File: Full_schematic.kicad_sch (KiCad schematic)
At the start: 165 parts, among them IC1 XC7A100T-1FTG256C, IC2 STM32U545VET6Q, J4 Conn_ST_STDC14, J5 Conn_ST_STDC14, SW1 SW_Nidec_CAS-120A1, U2 TPS54294PWP, U2 TPS54325PWPR, U3 SN74ALVC245PWR, U4 SN74ALVC245PWR, U5 STM32F745VGH6, Y1 ASCO, Y2 8MHz, Y3 8MHz

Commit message: koble vga-fpga
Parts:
- removed C62, C75: 1 uF, symbol Device:C
- removed C63, C65, C66, C67, C69, C76, C78, C79, C80, C81: 100 nF, symbol Device:C
- removed C64, C77: 4.7 uF, symbol Device:C
- removed C68, C70, C73, C74: 22pF, symbol Device:C
- removed C71, C72, C82, C83: 2.2u, symbol Device:C
- removed IC2: STM32U545VET6Q, QFP50P1600X1600X160-100N, symbol STM32U545VET6Q:STM32U545VET6Q
- removed J4, J5: Conn_ST_STDC14, symbol Connector:Conn_ST_STDC14
- removed R53, R54: 10k, symbol Device:R
- removed SW1: SW_Nidec_CAS-120A1, Button_Switch_SMD:Nidec_Copal_CAS-120A, symbol Switch:SW_Nidec_CAS-120A1
- removed U5: STM32F745VGH6, UFBGA100-7x7mm, symbol STM32F745VGH6:STM32F745VGH6
- removed Y2, Y3: 8MHz, symbol Device:Crystal_GND24
- added C84 (x2), C85, C86, C87 (x2), C88, C89, C90, C94: 100n, symbol Device:C
- added C85, C86: 1u, symbol Device:C
- added C88, C89: 6pF, symbol Device:C
- added C91: 10u, symbol Device:C
- added C92, C93: 2.2u, symbol Device:C
- added J6: Conn_ST_STDC14, symbol Connector:Conn_ST_STDC14
- added L5: 2.2u, symbol Device:L
- added R61, R62, R63, R64: 47, symbol Device:R
- added R65: 10k, symbol Device:R
- added SW2: SW_Nidec_CAS-120A1, Button_Switch_SMD:Nidec_Copal_CAS-120A, symbol Switch:SW_Nidec_CAS-120A1
- added U7: STM32U545VETxQ, Package_QFP:LQFP-100_14x14mm_P0.5mm, symbol MCU_ST_STM32U5:STM32U545VETxQ
- added Y4: 48MHz, symbol Device:Crystal_GND24
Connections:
- net +3.3V: now also C84.1, C85.1, C86.1, C87.1, C88.1, C89.1, C90.1, C91.1, J6.3 (VCC), SW2.1 (C)
- net CS(Acitive low): now also U7.66 (PC9)
- net GND: now also C84.2, C84.2, C85.2, C85.2, C86.1, C86.2, C87.1, C87.2, C88.2, C88.2, C89.2, C89.2, C90.2, C91.2, C92.2, C93.2, C94.2, J6.5 (GND), J6.7 (GND), SW2.3 (A), U7.10 (VSS), U7.19 (VSSA), U7.26 (VSS), U7.48 (VSSSMPS), U7.50 (VSS), U7.74 (VSS), U7.99 (VSS), Y4.2, Y4.4
- net MISO: now also U7.79 (PC11)
- net MOSI: now also U7.80 (PC12)
- net SCK: now also U7.78 (PC10)
- net VDD: now also U7.100 (VDD), U7.11 (VDD), U7.27 (VDD), U7.47 (VDDSMPS), U7.51 (VDD), U7.6 (VBAT), U7.75 (VDD)
- net at J2.2 (G1), R21.1, U4.7 (A6): now also IC1.M14 (IO_L4N_T0_D05_14)
- net at J2.1 (R0), R14.1, U3.2 (A1): now also IC1.T14 (IO_L10P_T1_D14_14)
- net at J2.10 (B3), R13.1, U3.9 (A8): now also IC1.R16 (IO_L9N_T1_DQS_D13_14)
- net at J2.3 (G2), R22.1, U4.8 (A7): now also IC1.K13 (IO_L5P_T0_D06_14)
- net at J2.2 (R1), R15.1, U3.3 (A2): now also IC1.T15 (IO_L10N_T1_D15_14)
- net at J2.3 (R2), R16.1, U3.4 (A3): now also IC1.N13 (IO_L11P_T1_SRCC_14)
- net at J2.4 (R3), R17.1, U3.5 (A4): now also IC1.P13 (IO_L11N_T1_SRCC_14)
- net at J2.7 (B0), R15.1, U3.6 (A5): now also IC1.P15 (IO_L8P_T1_D11_14)
- net at J2.8 (B1), R13.1, U3.7 (A6): now also IC1.P16 (IO_L8N_T1_D12_14)
- net at J2.9 (B2), R14.1, U3.8 (A7): now also IC1.R15 (IO_L9P_T1_DQS_14)
- net at J2.8 (VS), R18.1, U4.4 (A3): now also IC1.M16 (IO_L7P_T1_D09_14)
- net at IC1.L13 (IO_L5N_T0_D07_14): now also J2.4 (G3), R23.1, U4.9 (A8)
- net at IC1.L14 (IO_L4P_T0_D04_14): now also J2.1 (G0), R20.1, U4.6 (A5)
- net at IC1.N16 (IO_L7N_T1_D10_14): now also J2.7 (HS), R19.1, U4.5 (A4)
- new net: C94.1, U7.73 (VDDUSB)
- new net: L5.1, U7.46 (VLXSMPS)
- new net: C92.1, C93.1, L5.2, U7.49 (VDD11), U7.98 (VDD11)
- new net: C88.1, U7.12 (PH0), Y4.1
- new net: C89.1, U7.13 (PH1), Y4.3
- new net: J6.12 (~{RST}), U7.14 (NRST)
- new net: C86.2, C87.2, U7.20 (VREF+)
- new net: C84.1, C85.1, U7.21 (VDDA)
- new net: R62.1, U7.72 (PA13)
- new net: R61.1, U7.76 (PA14)
- new net: R64.1, U7.77 (PA15)
- new net: R63.1, U7.89 (PB3)
- new net: R65.2, U7.94 (PH3)
- new net: J6.8 (JTDO/SWO), R63.2
- new net: J6.4 (JTMS/SWDIO), R62.2
- new net: J6.6 (JCLK/SWCLK), R61.2
- new net: R65.1, SW2.2 (B)
- new net: J6.10 (JTDI/NC), R64.2
- no-connect marks 13 -> 9
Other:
- moved on the sheet: C1, C10, C11, C12, C13, C14, C15, C16, C17, C18, C19, C2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

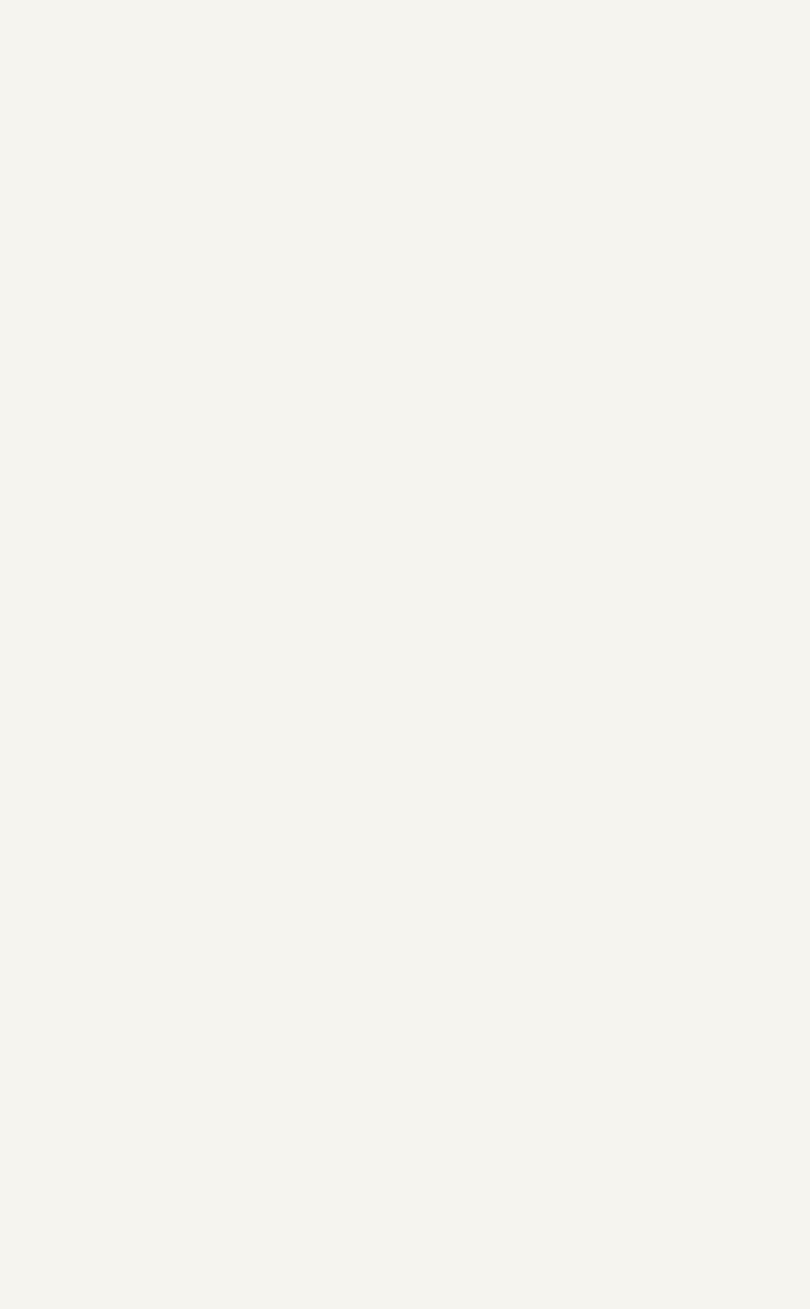
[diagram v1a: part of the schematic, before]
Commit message: Added display connector
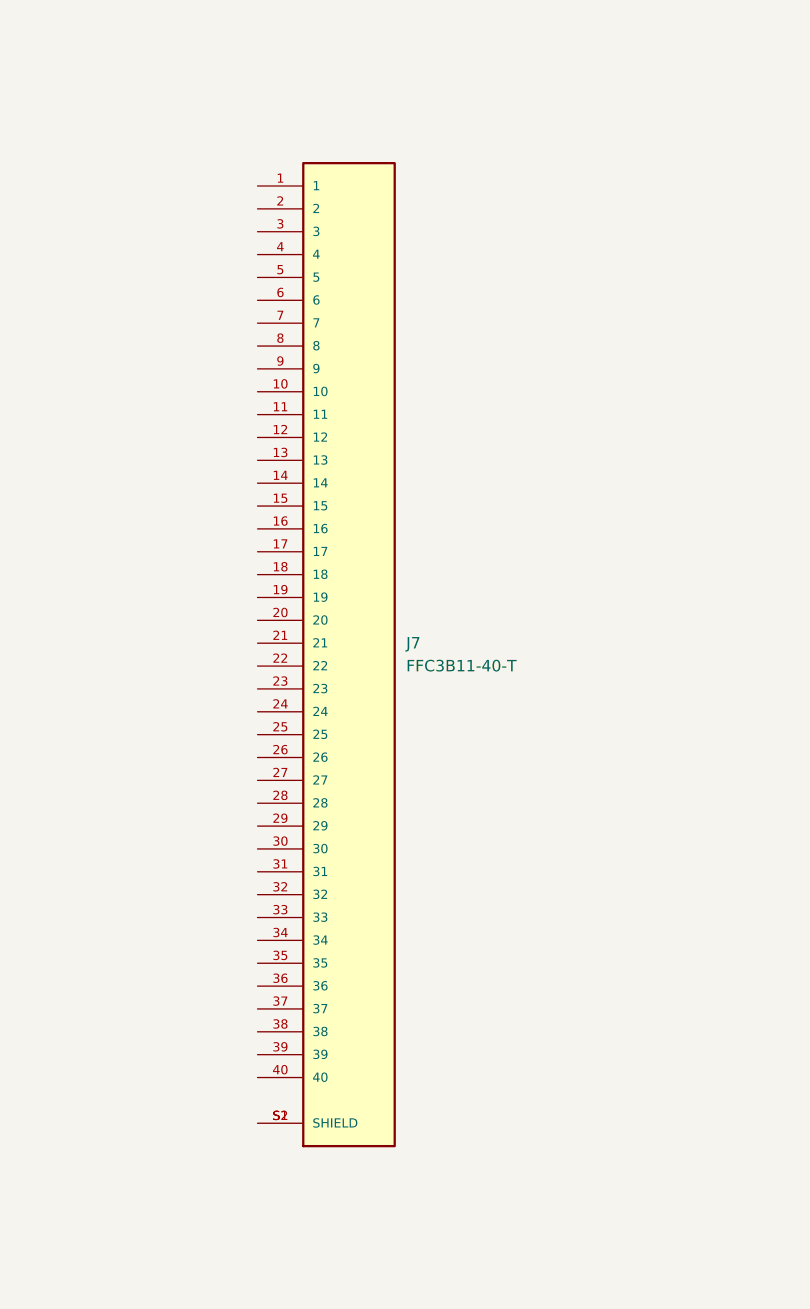
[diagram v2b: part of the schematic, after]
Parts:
- added J7: FFC3B11-40-T, FFC3B11-40-T:GCT_FFC3B11-40-T, symbol FFC3B11-40-T:FFC3B11-40-T
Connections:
- new net: J7.S1 (SHIELD), J7.S2 (SHIELD)

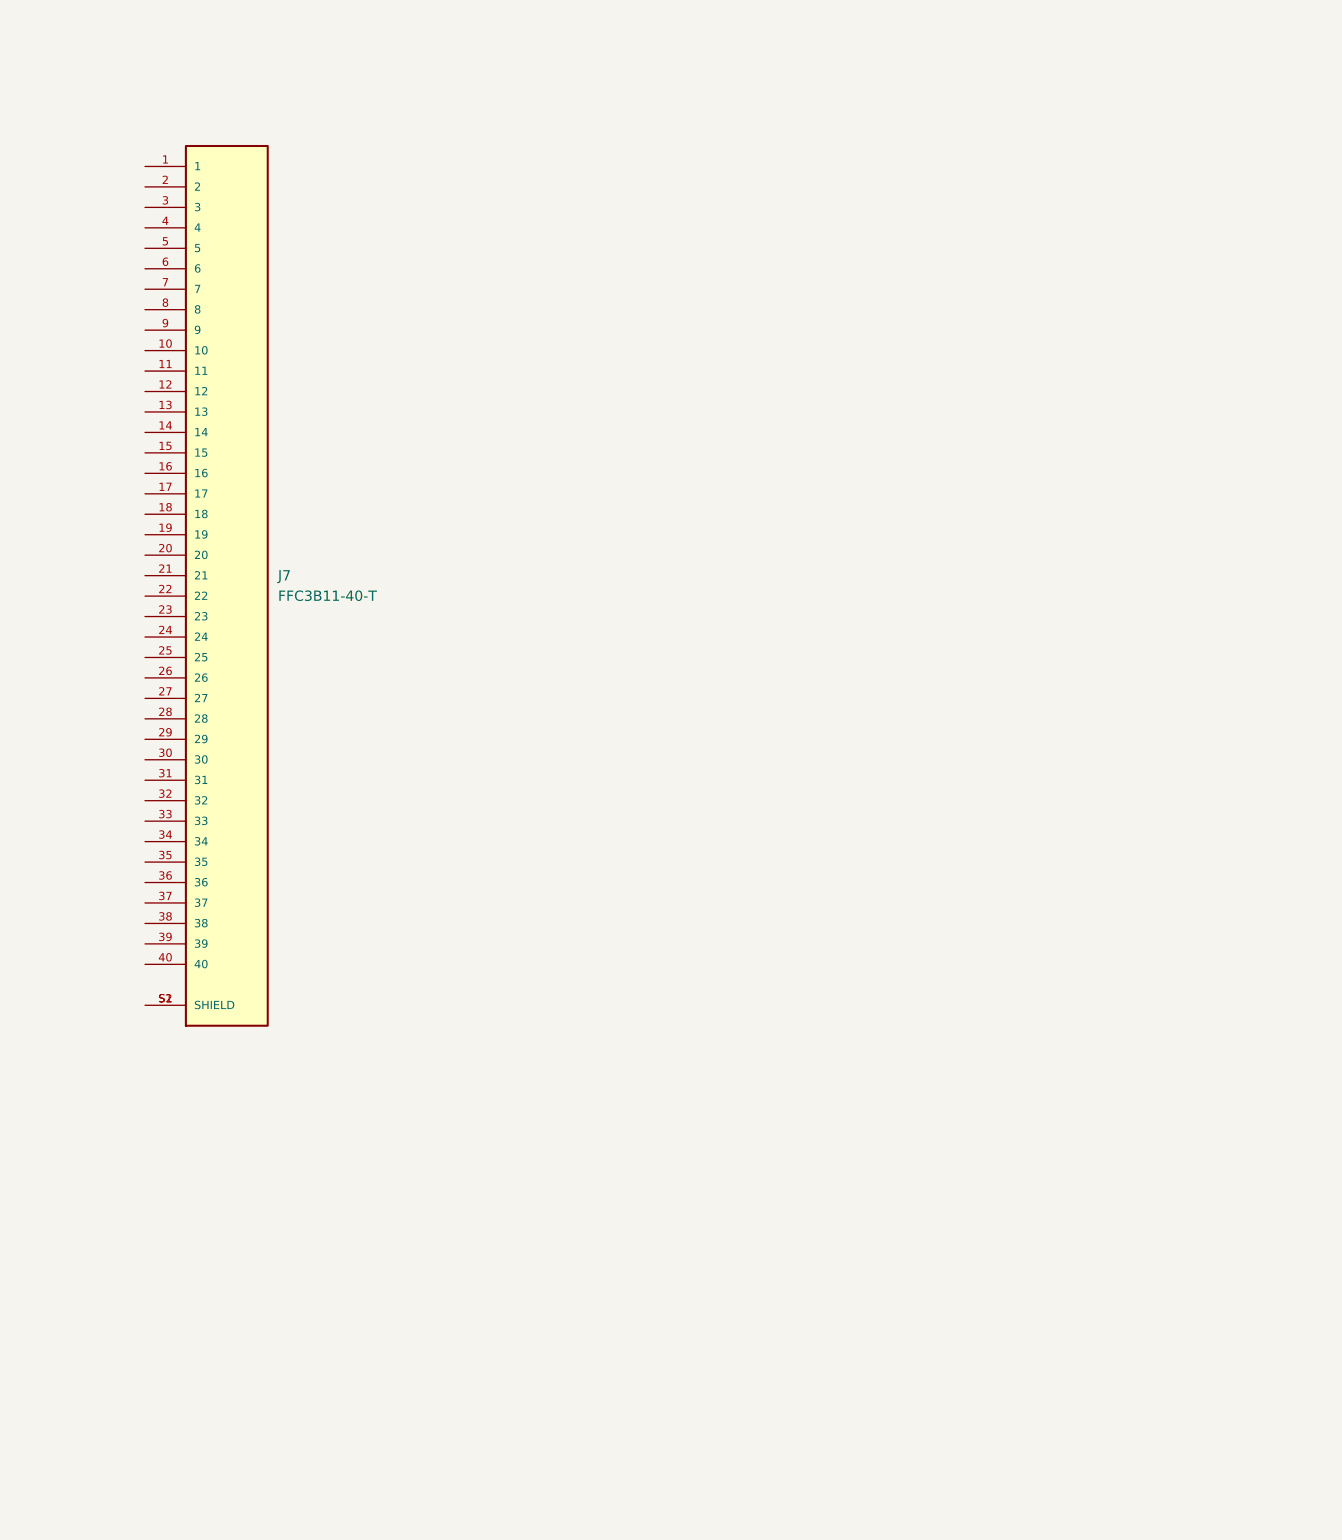
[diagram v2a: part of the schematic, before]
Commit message: Added display power supply to full schematic
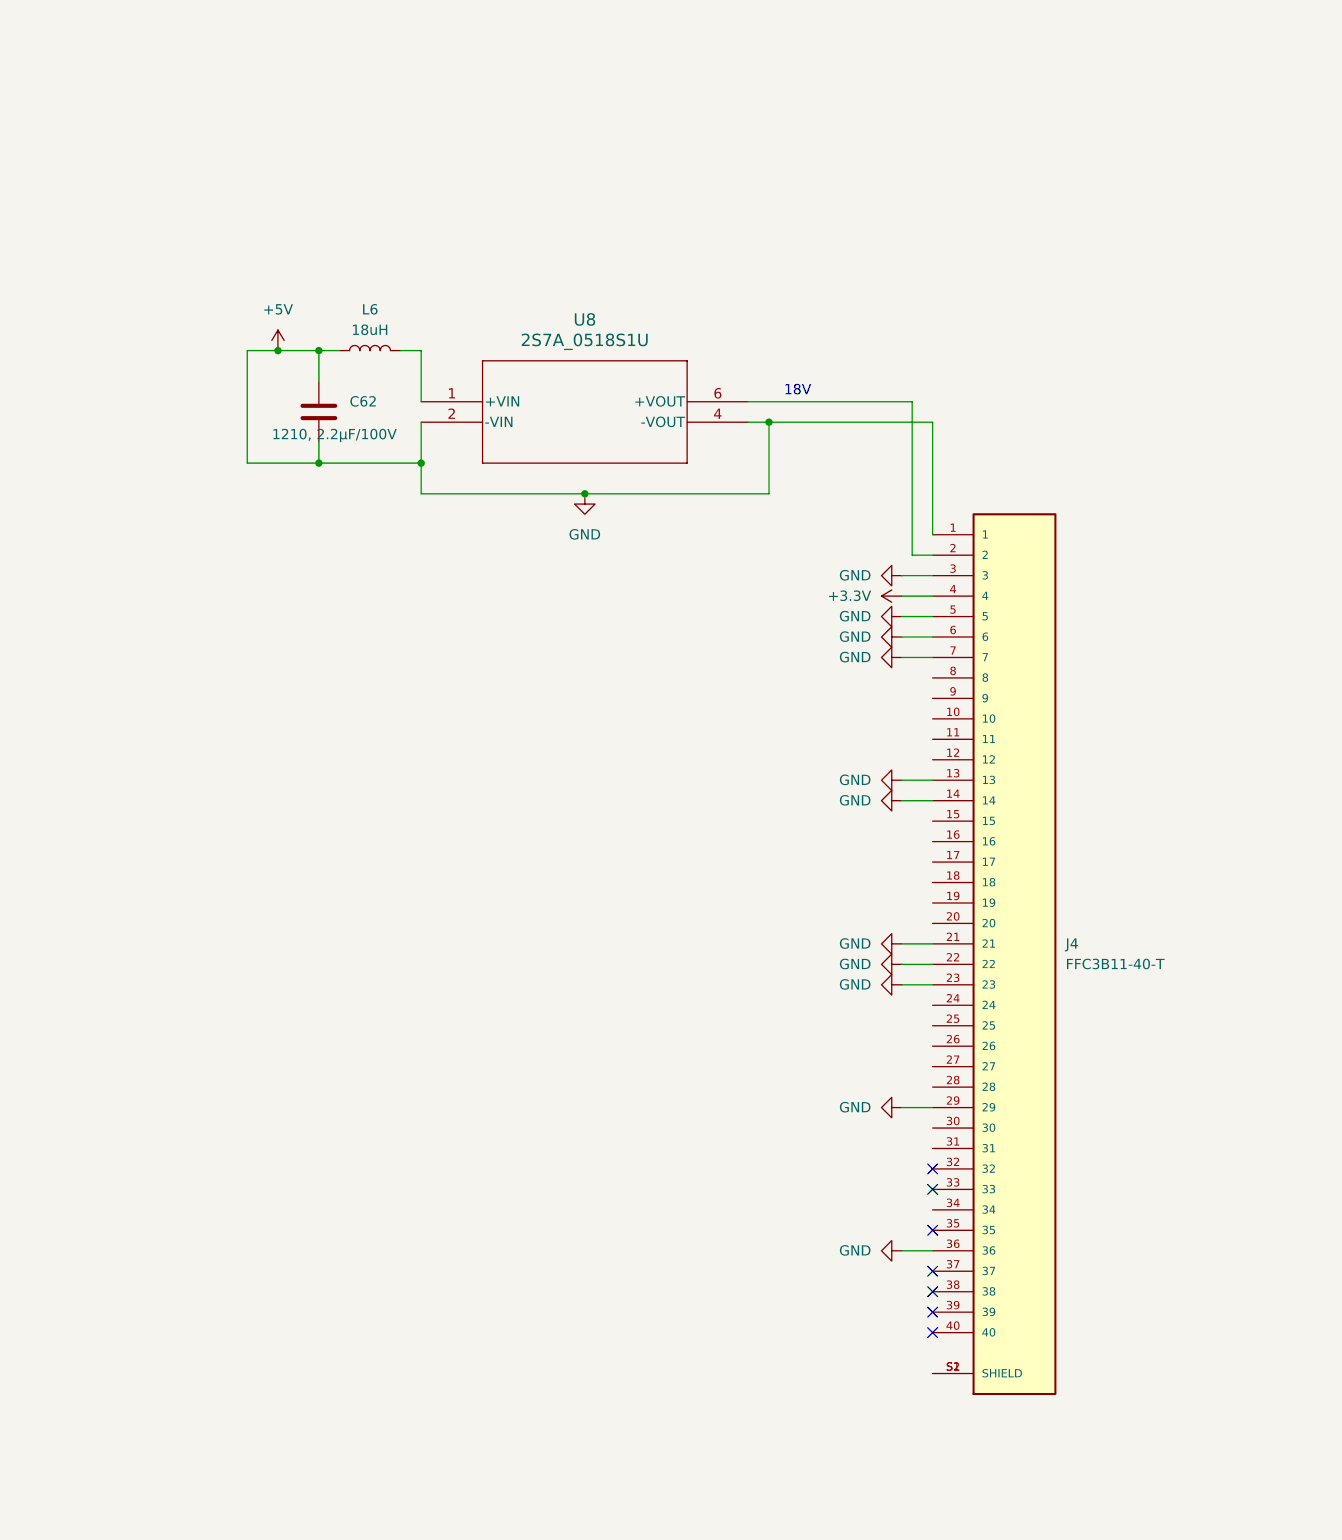
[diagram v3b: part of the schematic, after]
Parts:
- removed J7: FFC3B11-40-T, FFC3B11-40-T:GCT_FFC3B11-40-T, symbol FFC3B11-40-T:FFC3B11-40-T
- added C62: 1210, 2.2µF/100V, symbol Device:C
- added J4: FFC3B11-40-T, FFC3B11-40-T:GCT_FFC3B11-40-T, symbol FFC3B11-40-T:FFC3B11-40-T
- added L6: 18uH, symbol Device:L
- added U8: 2S7A_0518S1U, SIP4_2S7A_GAP, symbol 2S7A_0518S1U:2S7A_0518S1U
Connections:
- net +3.3V: now also J4.4
- net GND renamed +5V
- net +5V: now also C62.1, C62.2, J4.1, J4.13, J4.14, J4.21, J4.22, J4.23, J4.29, J4.3, J4.36, J4.5, J4.6, J4.7, L6.1, U8.2 (-VIN), U8.4 (-VOUT)
- new net: J4.2, U8.6 (+VOUT)
- new net: J4.S1 (SHIELD), J4.S2 (SHIELD)
- new net: L6.2, U8.1 (+VIN)
- no-connect marks 9 -> 16
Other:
- note added: "18V"

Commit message: Connected controllers and 7-segment display to mcu
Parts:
- removed SW2: SW_Nidec_CAS-120A1, Button_Switch_SMD:Nidec_Copal_CAS-120A, symbol Switch:SW_Nidec_CAS-120A1
- added R53, R67, R68, R69: 10k, symbol Device:R
- added R54, R55, R56, R57, R58, R59, R60, R70, R71, R72, R73, R74, R75, R76, R77, R78, R79, R80, R81, R82, R83, R84, R85, R86, R87, R88, R89: 220, symbol Device:R
- added R66: THB001P, THB001P_CNK, symbol THB001P:THB001P
- added SW3, SW4: SW_DPST_x2, symbol Switch:SW_DPST_x2
- added U10, U11, U13, U5: MC14511BDG, SOIC-16_ONS, symbol MC14511BDG:MC14511BDG
- added U12, U14, U6, U9: MAN72A, Display_7Segment:MAN72A, symbol Display_Character:MAN72A
- R65: value 10k -> 220
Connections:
- net +3.3V: now also R66.1, R66.1', R66.C, SW3.1 (A), SW4.1 (A), U10.16 (VDD), U10.3 (*LT), U10.4 (*BI), U11.16 (VDD), U11.3 (*LT), U11.4 (*BI), U12.14 (CA), U12.3 (CA), U13.16 (VDD), U13.3 (*LT), U13.4 (*BI), U14.14 (CA), U14.3 (CA), U5.16 (VDD), U5.3 (*LT), U5.4 (*BI), U6.14 (CA), U6.3 (CA), U9.14 (CA), U9.3 (CA); no longer C84.1, C85.1, C86.1, C87.1, C88.1, C89.1, C90.1, C91.1
- net +5V: now also R53.1, R66.3, R66.3', R67.2, R68.2, R69.2, U10.5 (LE), U10.8 (VSS), U11.5 (LE), U11.8 (VSS), U13.5 (LE), U13.8 (VSS), U5.5 (LE), U5.8 (VSS)
- net PC2: now reaches U7.17 (PC2)
- net PC2: now also R66.2
- net PC3: now reaches U7.18 (PC3)
- net PC3: now also R66.2'
- net PE9: now reaches U7.37 (PE9)
- net PE9: now also R66.B, R67.1
- net PE10: now reaches U7.38 (PE10)
- net PE10: now also R68.1, SW4.2 (B)
- net PE11: now reaches U7.39 (PE11)
- net PE11: now also R69.1, SW3.2 (B)
- net PB13: now reaches U7.52 (PB13)
- net PB13: now also U13.7 (A)
- net PB14: now reaches U7.53 (PB14)
- net PB14: now also U13.6 (D)
- net PB15: now reaches U7.54 (PB15)
- net PB15: now also U13.2 (C)
- net PD8: now reaches U7.55 (PD8)
- net PD8: now also U13.1 (B)
- net PD9: now reaches U7.56 (PD9)
- net PD9: now also U11.7 (A)
- net PD10: now reaches U7.57 (PD10)
- net PD10: now also U11.6 (D)
- net PD11: now reaches U7.58 (PD11)
- net PD11: now also U11.2 (C)
- net PD12: now reaches U7.59 (PD12)
- net PD12: now also U11.1 (B)
- net PD13: now reaches U7.60 (PD13)
- net PD13: now also U5.7 (A)
- net PD14: now reaches U7.61 (PD14)
- net PD14: now also U5.6 (D)
- net PD15: now reaches U7.62 (PD15)
- net PD15: now also U5.2 (C)
- net PC6: now reaches U7.63 (PC6)
- net PC6: now also U5.1 (B)
- net PC7: now reaches U7.64 (PC7)
- net PC7: now also U10.7 (A)
- net PC8: now reaches U7.65 (PC8)
- net PC8: now also U10.6 (D)
- net PA8: now reaches U7.67 (PA8)
- net PA8: now also U10.2 (C)
- net PA9: now reaches U7.68 (PA9)
- net PA9: now also U10.1 (B)
- net at R65.2: now also U12.1 (A); no longer U7.94 (PH3)
- net at R65.1: now also U11.13 (a)
- net VDD: no longer names the net of U7.100 (VDD), U7.11 (VDD), U7.27 (VDD), U7.47 (VDDSMPS), U7.51 (VDD), U7.6 (VBAT), U7.75 (VDD)
- net VDD: now also C84.1, C85.1, C86.1, C87.1, C88.1, C89.1, C90.1, C91.1
- new net: R70.2, U9.1 (A)
- new net: R72.2, U9.10 (C)
- new net: R76.2, U9.11 (G)
- new net: R71.2, U9.13 (B)
- new net: R75.2, U9.2 (F)
- new net: R74.2, U9.7 (E)
- new net: R73.2, U9.8 (D)
- new net: R56.1, U5.11 (c)
- new net: R56.2, U6.10 (C)
- new net: R78.1, U11.11 (c)
- new net: R78.2, U12.10 (C)
- new net: R77.1, U11.12 (b)
- new net: R77.2, U12.13 (B)
- new net: R74.1, U10.9 (e)
- new net: R57.1, U5.10 (d)
- new net: R57.2, U6.8 (D)
- new net: R86.1, U13.10 (d)
- new net: R86.2, U14.8 (D)
- new net: R73.1, U10.10 (d)
- new net: R79.1, U11.10 (d)
- new net: R82.1, U11.14 (g)
- new net: R81.1, U11.15 (f)
- new net: R80.1, U11.9 (e)
- new net: R83.2, U14.1 (A)
- new net: R85.2, U14.10 (C)
- new net: R89.2, U14.11 (G)
- new net: R84.2, U14.13 (B)
- new net: R88.2, U14.2 (F)
- new net: R87.2, U14.7 (E)
- new net: R79.2, U12.8 (D)
- new net: R54.2, U6.1 (A)
- new net: R60.2, U6.11 (G)
- new net: R55.2, U6.13 (B)
- new net: R59.2, U6.2 (F)
- new net: R58.2, U6.7 (E)
- new net: R85.1, U13.11 (c)
- new net: R80.2, U12.7 (E)
- new net: R54.1, U5.13 (a)
- new net: R60.1, U5.14 (g)
- new net: R55.1, U5.12 (b)
- new net: R76.1, U10.14 (g)
- new net: R53.2, U7.94 (PH3)
- new net: R59.1, U5.15 (f)
- new net: R58.1, U5.9 (e)
- new net: R82.2, U12.11 (G)
- new net: R71.1, U10.12 (b)
- new net: R72.1, U10.11 (c)
- new net: R70.1, U10.13 (a)
- new net: R75.1, U10.15 (f)
- new net: R87.1, U13.9 (e)
- new net: R88.1, U13.15 (f)
- new net: R83.1, U13.13 (a)
- new net: R84.1, U13.12 (b)
- new net: R89.1, U13.14 (g)
- new net: R81.2, U12.2 (F)
- no-connect marks 16 -> 22
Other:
- moved on the sheet: C61, C62, C84, C85, C86, C87, C88, C89, C90, C91, C92, C93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
